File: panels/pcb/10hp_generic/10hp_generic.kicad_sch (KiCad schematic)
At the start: 81 parts, among them J1 Conn_02x04_Odd_Even, J2 SWD, SW1 SW_Push, SW10 SW_Push, SW11 SW_Push, SW12 SW_Push, SW13 SW_Push, SW14 SW_Push, SW15 SW_Push, SW16 SW_Push, SW2 SW_Push, SW3 SW_Push, SW4 SW_Push, SW5 SW_Push, SW6 SW_Push, SW7 SW_Push, SW8 SW_Push, SW9 SW_Push, U1 STM32F072RBTx, U2 AMS1117-3.3

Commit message: PCB design for generic r3 (wip)
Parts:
- removed U1: STM32F072RBTx, Package_QFP:LQFP-64_10x10mm_P0.5mm, symbol MCU_ST_STM32F0:STM32F072RBTx
- added C38, C39: 20pF, Capacitor_SMD:C_0603_1608Metric, symbol Device:C
- added C40: 100nF, Capacitor_SMD:C_0402_1005Metric, symbol Device:C
- added C41: 100pF, Capacitor_SMD:C_0402_1005Metric, symbol Device:C
- added R1: 10K, Resistor_SMD:R_0402_1005Metric, symbol Device:R
- added U1: TJA1051T-3, Package_SO:SOIC-8_3.9x4.9mm_P1.27mm, symbol Interface_CAN_LIN:TJA1051T-3
- added U3: STM32F103C8Tx, Package_QFP:LQFP-48_7x7mm_P0.5mm, symbol MCU_ST_STM32F1:STM32F103C8Tx
- added Y1: 8MHz, riban:HC-49S, symbol Device:Crystal
- J1: value Conn_02x04_Odd_Even -> CAN_PWR; footprint Connector_IDC:IDC-Header_2x04_P2.54mm_Vertical -> Connector_IDC:IDC-Header_2x03_P2.54mm_Vertical; symbol Connector_Generic:Conn_02x04_Odd_Even -> Connector_Generic:Conn_02x03_Odd_Even; LCSC C146619 -> (none)
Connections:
- net DETECT is gone; now on net GND: J1.5 (Pin_5)
- net RESET is gone; now on net GND: J1.6 (Pin_6)
- net +5V: now also C40.1, U1.2 (GND)
- net GND: now also C38.1, C39.1, C40.2, C41.1, U1.3 (VCC), U1.8 (S), U3.23 (VSS), U3.35 (VSS), U3.44 (BOOT0), U3.47 (VSS), U3.8 (VSSA); no longer J1.7 (Pin_7), J1.8 (Pin_8)
- net POT1: now also U3.17 (PA7)
- net POT2: now also U3.16 (PA6)
- net POT3: now also U3.15 (PA5)
- net POT4: now also U3.14 (PA4)
- net POT5: now also U3.13 (PA3)
- net POT6: now also U3.10 (PA0)
- net POT7: now also U3.12 (PA2)
- net POT8: now also U3.11 (PA1)
- net SCL: now also U3.43 (PB7); no longer J1.3 (Pin_3)
- net SDA: now also U3.42 (PB6); no longer J1.4 (Pin_4)
- net SW1: now also U3.26 (PB13)
- net SW2: now also U3.27 (PB14)
- net SW3: now also U3.30 (PA9)
- net SW4: now also U3.31 (PA10)
- net SW5: now also U3.22 (PB11)
- net SW6: now also U3.25 (PB12)
- net SW7: now also U3.32 (PA11)
- net SW8: now also U3.33 (PA12)
- net SWCLK: now also U3.37 (PA14)
- net SWDIO: now also U3.34 (PA13)
- net VDD: now also R1.2, U3.1 (VBAT), U3.24 (VDD), U3.36 (VDD), U3.48 (VDD), U3.9 (VDDA)
- net WS2812: now also U3.28 (PB15)
- new net: C39.2, U3.6 (PD1), Y1.1
- new net: C41.2, R1.1, U3.7 (NRST)
- new net: C38.2, U3.5 (PD0), Y1.2
- new net: U1.1 (TXD), U3.46 (PB9)
- new net: U1.4 (RXD), U3.45 (PB8)
- new net CAN-H: J1.3 (Pin_3), U1.6 (CANL)
- new net CAN-L: J1.4 (Pin_4), U1.7 (CANH)
- no-connect marks 31 -> 13
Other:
- moved on the sheet: C24, C25, C26, C27, C28, C29, C30, C31

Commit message: Rev 3 boards complete - probably
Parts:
- added J3: I2C, Connector_PinHeader_2.54mm:PinHeader_1x04_P2.54mm_Vertical, symbol Connector_Generic:Conn_01x04
- C38, C39: value 20pF -> 22pF; LCSC C91702 -> C326840
- C41: LCSC C1525 -> C1546
- D1, D10, D11, D12, D13, D14, D15, D16, D2, D3, D4, D5, D6, D7, D8, D9: footprint WS2812:XL-2121RGBC-WS2812B -> riban:LED_XL-1615RGBC-WS2812B; symbol WS2812:XL-2121RGBC-WS2812B -> ws2812b:WS2812B; LCSC C5349957 -> C5349954
- J2, RV1, RV2, RV3, RV4, RV5, RV6, RV7, RV8: now left out of the parts list
- SW1, SW10, SW11, SW12, SW13, SW14, SW15, SW16, SW2, SW3, SW4, SW5, SW6, SW7, SW8, SW9: footprint Button_Switch_THT:SW_PUSH_6mm_H4.3mm -> riban:SW_PUSH_6mm_H4.3mm; now left out of the parts list
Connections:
- net +5V: now also D1.2 (VDD), D10.2 (VDD), D11.2 (VDD), D12.2 (VDD), D13.2 (VDD), D14.2 (VDD), D15.2 (VDD), D16.2 (VDD), D2.2 (VDD), D3.2 (VDD), D4.2 (VDD), D5.2 (VDD), D6.2 (VDD), D7.2 (VDD), D8.2 (VDD), D9.2 (VDD), J3.4 (Pin_4); no longer D1.3 (VDD), D10.3 (VDD), D11.3 (VDD), D12.3 (VDD), D13.3 (VDD), D14.3 (VDD), D15.3 (VDD), D16.3 (VDD), D2.3 (VDD), D3.3 (VDD), D4.3 (VDD), D5.3 (VDD), D6.3 (VDD), D7.3 (VDD), D8.3 (VDD), D9.3 (VDD)
- net GND: now also D1.3 (VSS), D10.3 (VSS), D11.3 (VSS), D12.3 (VSS), D13.3 (VSS), D14.3 (VSS), D15.3 (VSS), D16.3 (VSS), D2.3 (VSS), D3.3 (VSS), D4.3 (VSS), D5.3 (VSS), D6.3 (VSS), D7.3 (VSS), D8.3 (VSS), D9.3 (VSS), J3.1 (Pin_1); no longer D1.1 (VSS), D10.1 (VSS), D11.1 (VSS), D12.1 (VSS), D13.1 (VSS), D14.1 (VSS), D15.1 (VSS), D16.1 (VSS), D2.1 (VSS), D3.1 (VSS), D4.1 (VSS), D5.1 (VSS), D6.1 (VSS), D7.1 (VSS), D8.1 (VSS), D9.1 (VSS)
- net SCL: now also U3.42 (PB6), J3.2 (Pin_2); no longer U3.43 (PB7)
- net SDA: now also U3.43 (PB7), J3.3 (Pin_3); no longer U3.42 (PB6)
- net SWCLK: now also J2.3 (Pin_3); no longer J2.2 (Pin_2)
- net SWDIO: now also J2.2 (Pin_2); no longer J2.3 (Pin_3)
- net WS2812: now also D1.4 (DIN); no longer D1.2 (DIN)
- net at D2.4 (DIN): now also D1.1 (DOUT); no longer D3.2 (DIN)
- net at D3.4 (DIN): now also D2.1 (DOUT); no longer D4.2 (DIN)
- net at D4.4 (DIN): now also D3.1 (DOUT); no longer D5.2 (DIN)
- net at D5.4 (DIN): now also D4.1 (DOUT); no longer D6.2 (DIN)
- net at D6.4 (DIN): now also D5.1 (DOUT); no longer D7.2 (DIN)
- net at D7.4 (DIN): now also D6.1 (DOUT); no longer D8.2 (DIN)
- net at D8.4 (DIN): now also D7.1 (DOUT); no longer D9.2 (DIN)
- net at D9.4 (DIN): now also D8.1 (DOUT); no longer D10.2 (DIN)
- net at D10.4 (DIN): now also D9.1 (DOUT); no longer D11.2 (DIN)
- net at D11.4 (DIN): now also D10.1 (DOUT); no longer D12.2 (DIN)
- net at D13.4 (DIN): now also D12.1 (DOUT); no longer D14.2 (DIN)
- net at D14.4 (DIN): now also D13.1 (DOUT); no longer D15.2 (DIN)
- net at D12.4 (DIN): now also D11.1 (DOUT); no longer D13.2 (DIN)
- net at D15.4 (DIN): now also D14.1 (DOUT); no longer D16.2 (DIN)
- net at D16.4 (DIN): now also D15.1 (DOUT)
- no-connect marks 13 -> 14

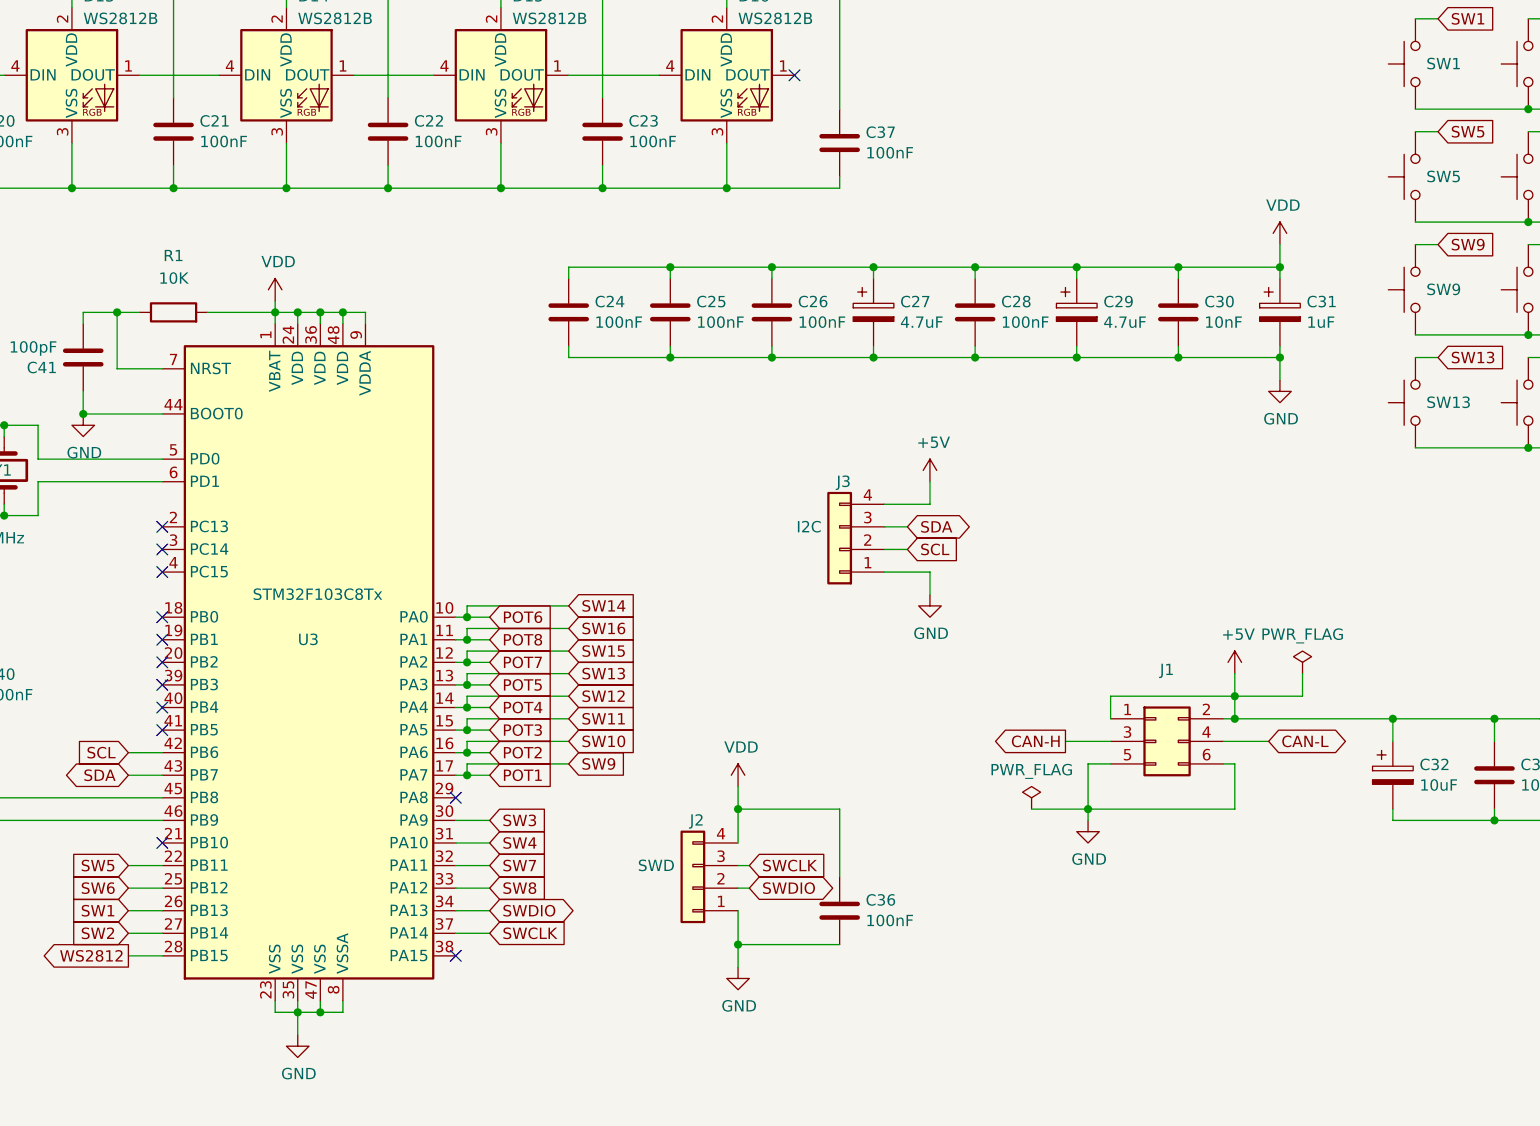
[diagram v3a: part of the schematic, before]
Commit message: R3 PCB and front panel
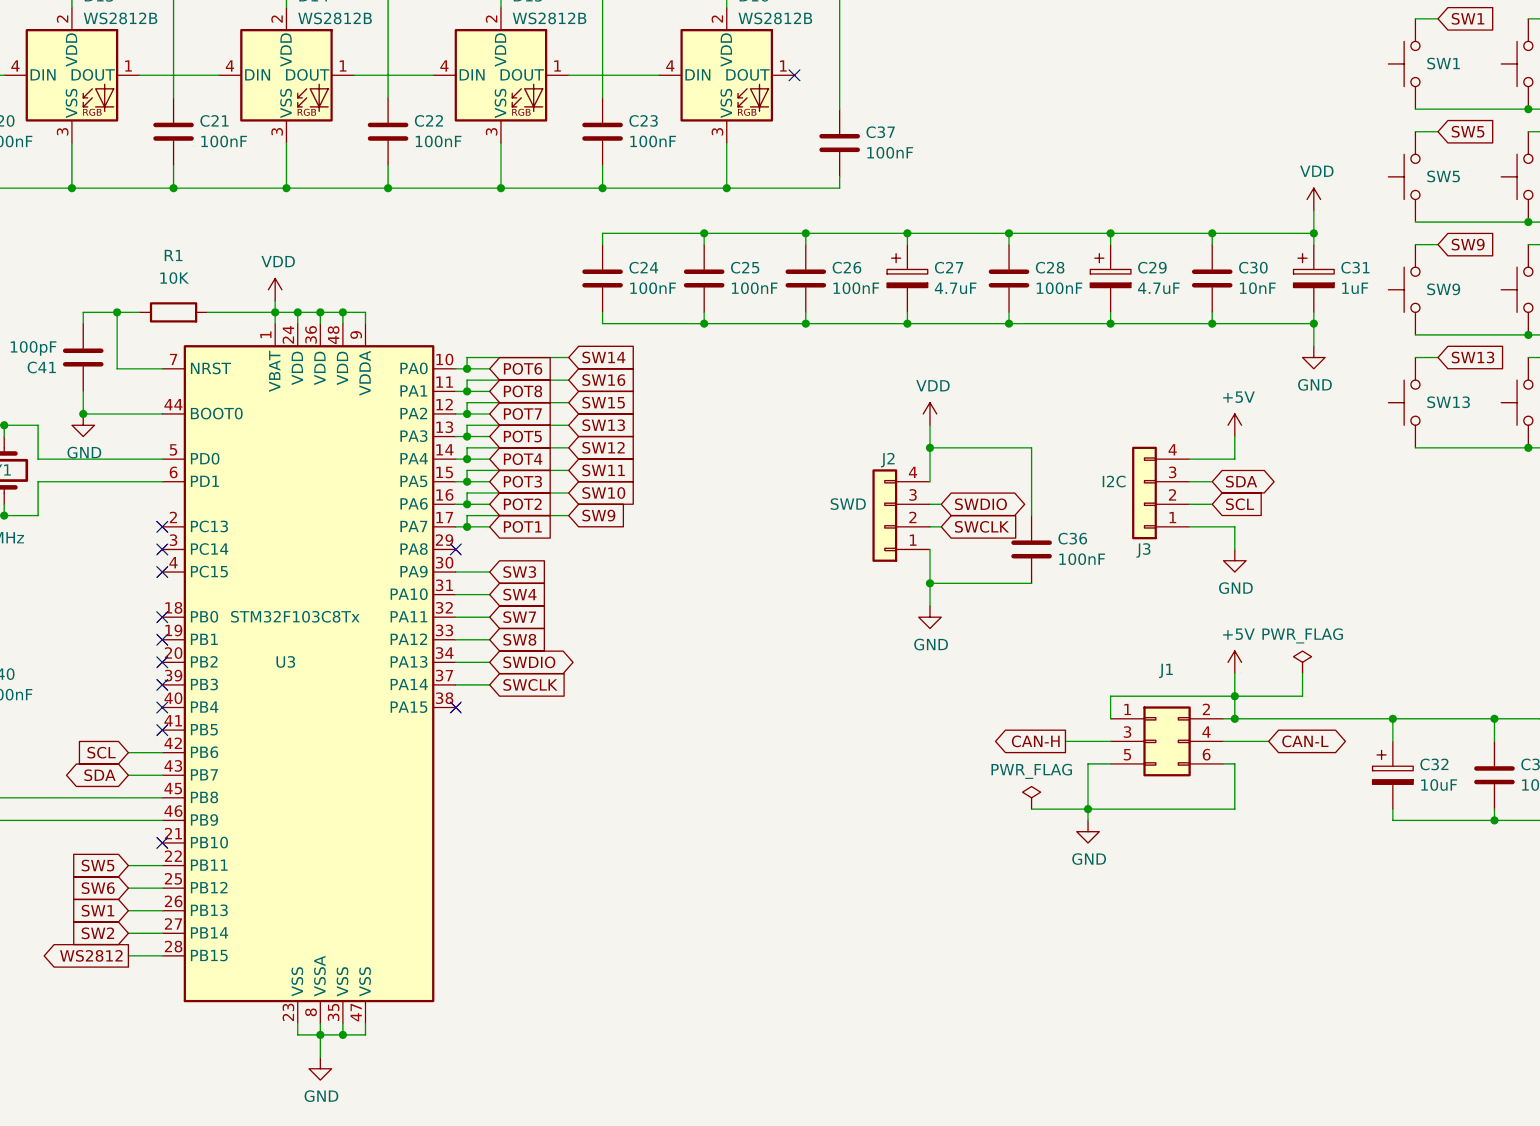
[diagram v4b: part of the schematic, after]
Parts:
- RV1, RV2, RV3, RV4, RV5, RV6, RV7, RV8: symbol Device:R_POT -> Device:R_Potentiometer
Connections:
- net SWCLK: now also J2.2 (Pin_2); no longer J2.3 (Pin_3)
- net SWDIO: now also J2.3 (Pin_3); no longer J2.2 (Pin_2)
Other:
- moved on the sheet: C24, C25, C26, C27, C28, C29, C30, C31, C36, J2, J3, U3

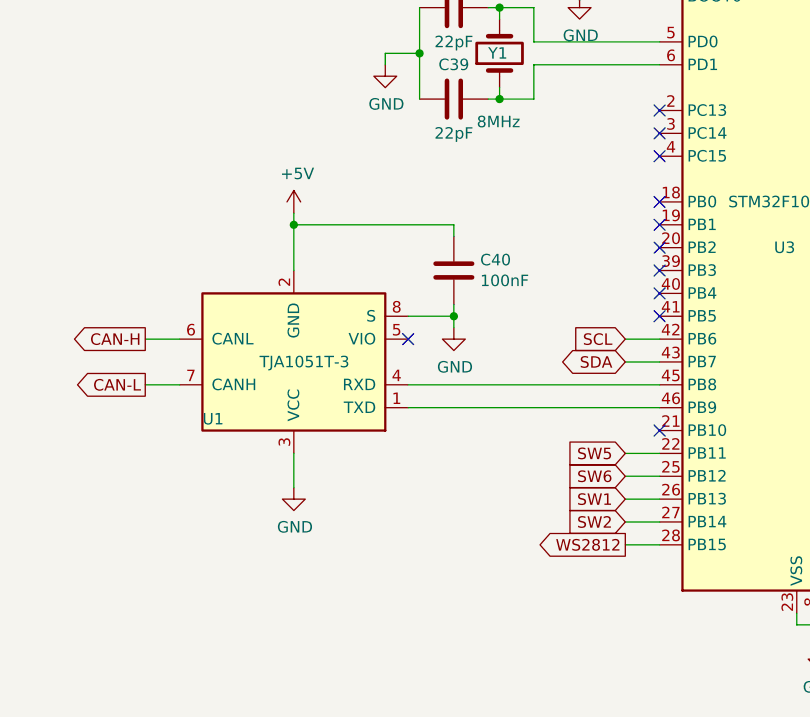
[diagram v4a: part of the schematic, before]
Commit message: Updated PCB fixing issues with r3:   Reversed power pins on U1.   Increase size of potentiometer anchors holes. Enable external high speed clock. Enable all LEDs, switches and pots.
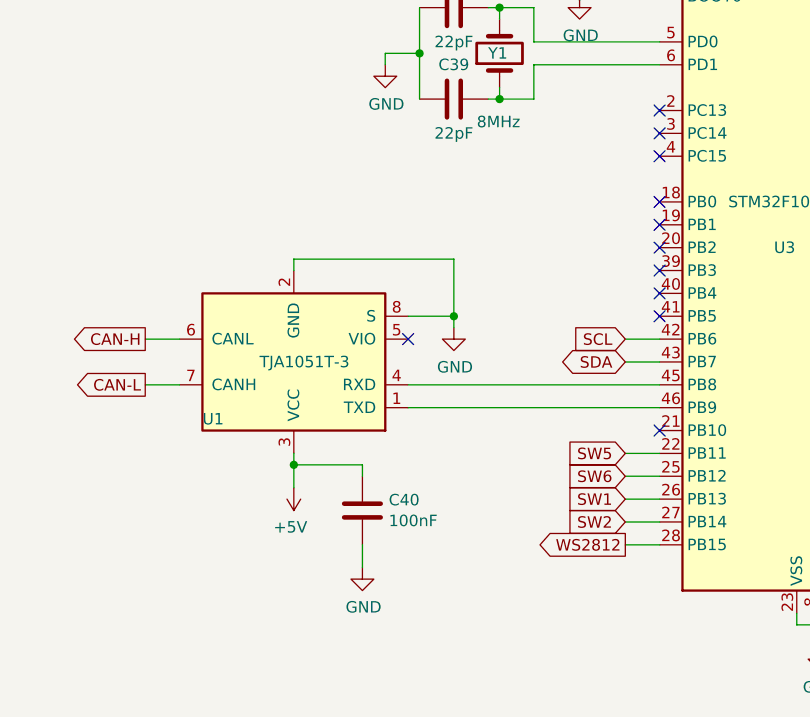
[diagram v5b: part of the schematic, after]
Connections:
- net +5V: now also U1.3 (VCC); no longer U1.2 (GND)
- net GND: now also U1.2 (GND); no longer U1.3 (VCC)
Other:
- moved on the sheet: C40
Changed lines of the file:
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@@
 (kicad_sch
-	(version 20231120)
+	(version 20240101)
 	(generator "eeschema")
-	(generator_version "8.0")
+	(generator_version "8.99")
 	(paper "A4")
 	(title_block
 		(title "riban modular 10HP generic panel")
-		(date "2024-03-08")
-		(rev "3")
+		(date "2024-03-31")
+		(rev "4")
 		(company "riban")
 	)
@@
 	)
 	(junction
+		(at 49.53 162.56)
+		(diameter 0)
+		(color 0 0 0 0)
+	)
+	(junction
 		(at 224.79 34.29)
 		(diameter 0)
@@
 	)
 	(junction
-		(at 49.53 135.89)
-		(diameter 0)
-		(color 0 0 0 0)
-	)
-	(junction
 		(at 115.57 34.29)
 		(diameter 0)
@@
 	(wire
 		(pts
+			(xy 49.53 162.56) (xy 57.15 162.56)
+		)
+		(stroke
+			(width 0)
+			(type default)
+		)
+	)
+	(wire
+		(pts
 			(xy 123.19 118.11) (xy 124.46 118.11)
 		)
@@
 	(wire
 		(pts
-			(xy 110.49 180.34) (xy 113.03 180.34)
+			(xy 67.31 139.7) (xy 67.31 146.05)
 		)
 		(stroke
@@
 	(wire
 		(pts
-			(xy 153.67 60.96) (xy 166.37 60.96)
+			(xy 110.49 180.34) (xy 113.03 180.34)
 		)
 		(stroke
@@
 	(wire
 		(pts
-			(xy 240.03 156.21) (xy 252.73 156.21)
+			(xy 153.67 60.96) (xy 166.37 60.96)
 		)
 		(stroke
@@
 	(wire
 		(pts
-			(xy 210.82 154.94) (xy 194.31 154.94)
+			(xy 240.03 156.21) (xy 252.73 156.21)
 		)
 		(stroke
@@
 	(wire
 		(pts
-			(xy 63.5 116.84) (xy 59.69 116.84)
+			(xy 210.82 154.94) (xy 194.31 154.94)
 		)
 		(stroke
@@
 	(wire
 		(pts
-			(xy 54.61 29.21) (xy 71.12 29.21)
+			(xy 63.5 116.84) (xy 59.69 116.84)
 		)
 		(stroke
@@
 	(wire
 		(pts
-			(xy 107.95 180.34) (xy 107.95 182.88)
+			(xy 54.61 29.21) (xy 71.12 29.21)
 		)
 		(stroke
@@
 	(wire
 		(pts
-			(xy 208.28 45.72) (xy 217.17 45.72)
+			(xy 107.95 180.34) (xy 107.95 182.88)
 		)
 		(stroke
@@
 	(wire
 		(pts
-			(xy 67.31 144.78) (xy 67.31 146.05)
+			(xy 208.28 45.72) (xy 217.17 45.72)
 		)
 		(stroke
@@
 	(wire
 		(pts
-			(xy 49.53 135.89) (xy 49.53 140.97)
-		)
-		(stroke
-			(width 0)
-			(type default)
-		)
-	)
-	(wire
-		(pts
 			(xy 262.89 154.94) (xy 262.89 156.21)
 		)
@@
 	(wire
 		(pts
-			(xy 49.53 135.89) (xy 67.31 135.89)
+			(xy 107.95 180.34) (xy 105.41 180.34)
 		)
 		(stroke
@@
 	(wire
 		(pts
-			(xy 107.95 180.34) (xy 105.41 180.34)
+			(xy 85.09 105.41) (xy 85.09 99.06)
 		)
 		(stroke
@@
 	(wire
 		(pts
-			(xy 85.09 105.41) (xy 85.09 99.06)
+			(xy 91.44 34.29) (xy 104.14 34.29)
 		)
 		(stroke
@@
 	(wire
 		(pts
-			(xy 91.44 34.29) (xy 104.14 34.29)
+			(xy 91.44 58.42) (xy 104.14 58.42)
 		)
 		(stroke
@@
 	(wire
 		(pts
-			(xy 91.44 58.42) (xy 104.14 58.42)
+			(xy 163.83 55.88) (xy 163.83 58.42)
 		)
 		(stroke
@@
 	(wire
 		(pts
-			(xy 163.83 55.88) (xy 163.83 58.42)
+			(xy 127 113.03) (xy 124.46 113.03)
 		)
 		(stroke
@@
 	(wire
 		(pts
-			(xy 127 113.03) (xy 124.46 113.03)
+			(xy 49.53 140.97) (xy 49.53 139.7)
 		)
 		(stroke
@@
 	(wire
 		(pts
-			(xy 49.53 134.62) (xy 49.53 135.89)
-		)
-		(stroke
-			(width 0)
-			(type default)
-		)
-	)
-	(wire
-		(pts
 			(xy 187.96 154.94) (xy 194.31 154.94)
 		)
@@
 	(wire
 		(pts
+			(xy 49.53 139.7) (xy 67.31 139.7)
+		)
+		(stroke
+			(width 0)
+			(type default)
+		)
+	)
+	(wire
+		(pts
 			(xy 27.94 60.96) (xy 31.75 60.96)
 		)
@@
 	(wire
 		(pts
-			(xy 31.75 60.96) (xy 43.18 60.96)
+			(xy 49.53 162.56) (xy 49.53 165.1)
 		)
 		(stroke
@@
 	(wire
 		(pts
-			(xy 139.7 99.06) (xy 139.7 100.33)
+			(xy 31.75 60.96) (xy 43.18 60.96)
 		)
 		(stroke
@@
 	(wire
 		(pts
-			(xy 127 123.19) (xy 124.46 123.19)
+			(xy 139.7 99.06) (xy 139.7 100.33)
 		)
 		(stroke
@@
 	(wire
 		(pts
-			(xy 269.24 114.3) (xy 279.4 114.3)
+			(xy 127 123.19) (xy 124.46 123.19)
 		)
 		(stroke
@@
 	(wire
 		(pts
-			(xy 274.32 144.78) (xy 274.32 139.7)
+			(xy 269.24 114.3) (xy 279.4 114.3)
 		)
 		(stroke
@@
 	(wire
 		(pts
-			(xy 124.46 105.41) (xy 123.19 105.41)
+			(xy 274.32 144.78) (xy 274.32 139.7)
 		)
 		(stroke
@@
 	(wire
 		(pts
-			(xy 67.31 135.89) (xy 67.31 137.16)
+			(xy 124.46 105.41) (xy 123.19 105.41)
 		)
 		(stroke
@@
 	(wire
 		(pts
+			(xy 57.15 171.45) (xy 57.15 173.99)
+		)
+		(stroke
+			(width 0)
+			(type default)
+		)
+	)
+	(wire
+		(pts
 			(xy 173.99 91.44) (xy 173.99 90.17)
 		)
@@
 	(wire
 		(pts
+			(xy 57.15 163.83) (xy 57.15 162.56)
+		)
+		(stroke
+			(width 0)
+			(type default)
+		)
+	)
+	(wire
+		(pts
 			(xy 135.89 72.39) (xy 146.05 72.39)
 		)
@@
 	(wire
 		(pts
-			(xy 49.53 161.29) (xy 49.53 165.1)
+			(xy 49.53 161.29) (xy 49.53 162.56)
 		)
 		(stroke
@@
 	(symbol
 		(lib_id "power:GND")
-		(at 49.53 165.1 0)
+		(at 57.15 173.99 0)
 		(unit 1)
 		(exclude_from_sim no)
@@
 		(dnp no)
 		(property "Reference" "#PWR020"
-			(at 49.53 171.45 0)
+			(at 57.15 180.34 0)
 			(effects
 				(font
@@
 		)
 		(property "Value" "GND"
-			(at 49.657 169.4942 0)
+			(at 57.277 178.3842 0)
 			(effects
 				(font
@@
 		)
 		(property "Footprint" ""
-			(at 49.53 165.1 0)
+			(at 57.15 173.99 0)
 			(effects
 				(font
@@
 		)
 		(property "Datasheet" ""
-			(at 49.53 165.1 0)
+			(at 57.15 173.99 0)
 			(effects
 				(font
@@
 		)
 		(property "Description" ""
-			(at 49.53 165.1 0)
+			(at 57.15 173.99 0)
 			(effects
 				(font
@@
 	(symbol
 		(lib_id "Device:C")
-		(at 67.31 140.97 0)
+		(at 57.15 167.64 0)
 		(unit 1)
 		(exclude_from_sim no)
@@
 		(dnp no)
 		(property "Reference" "C40"
-			(at 70.231 139.8016 0)
+			(at 60.071 166.4716 0)
 			(effects
 				(font
@@
 		)
 		(property "Value" "100nF"
-			(at 70.231 142.113 0)
+			(at 60.071 168.783 0)
 			(effects
 				(font
@@
 		)
 		(property "Footprint" "Capacitor_SMD:C_0402_1005Metric"
-			(at 68.2752 144.78 0)
+			(at 58.1152 171.45 0)
 			(effects
 				(font
@@
 		)
 		(property "Datasheet" "~"
-			(at 67.31 140.97 0)
+			(at 57.15 167.64 0)
 			(effects
 				(font
@@
 		)
 		(property "Description" ""
-			(at 67.31 140.97 0)
+			(at 57.15 167.64 0)
 			(effects
 				(font
@@
 		)
 		(property "LCSC" "C1525"
-			(at 67.31 140.97 0)
+			(at 57.15 167.64 0)
 			(effects
 				(font
@@
 	(symbol
 		(lib_id "power:+5V")
-		(at 49.53 134.62 0)
+		(at 49.53 165.1 180)
 		(unit 1)
 		(exclude_from_sim no)
@@
 		(dnp no)
 		(property "Reference" "#PWR019"
-			(at 49.53 138.43 0)
+			(at 49.53 161.29 0)
 			(effects
 				(font
@@
 		)
 		(property "Value" "+5V"
-			(at 49.911 130.2258 0)
+			(at 49.149 169.4942 0)
 			(effects
 				(font
@@
 		)
 		(property "Footprint" ""
-			(at 49.53 134.62 0)
+			(at 49.53 165.1 0)
 			(effects
 				(font
@@
 		)
 		(property "Datasheet" ""
-			(at 49.53 134.62 0)
+			(at 49.53 165.1 0)
 			(effects
 				(font
@@
 		)
 		(property "Description" ""
-			(at 49.53 134.62 0)
+			(at 49.53 165.1 0)
 			(effects
 				(font
